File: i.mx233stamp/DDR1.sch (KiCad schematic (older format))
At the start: 15 parts, among them U2 MT46V32M16TG

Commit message: Added some connections to the pin header and the filters of the sources
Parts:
- removed C22, C23, C24, C25, C26, C27, C28, C29: 100nF, 0402, symbol CAP
- removed C30: 1uF, 0603, symbol CAP
- removed RP1, RP2, RP3, RP4, RP5: R_PACK4, R_PACK4-0402, symbol R_PACK4
- added C? (x10): 0.1uF, symbol C
- added C?: 1uF, symbol C
- added R? (x2): 1K 1%, symbol R
- added R?: 47K, symbol R
- added R?: R, symbol R
- added U?: M25P32, symbol M25P32
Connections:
- net labels added: SSPI_CMD, SSPI_DATA0, SSPI_DATA1, SSPI_DATA2, SSPI_DATA3, SSPI_SCK, VDDIO_3V3, VDDM_2V5
- net labels removed: R_DDR_A0, R_DDR_A1, R_DDR_A10, R_DDR_A11, R_DDR_A12, R_DDR_A2, R_DDR_A3, R_DDR_A4, R_DDR_A5, R_DDR_A6, R_DDR_A7, R_DDR_A8, R_DDR_A9
- wire segments 125 -> 136
- no-connect marks 0 -> 7

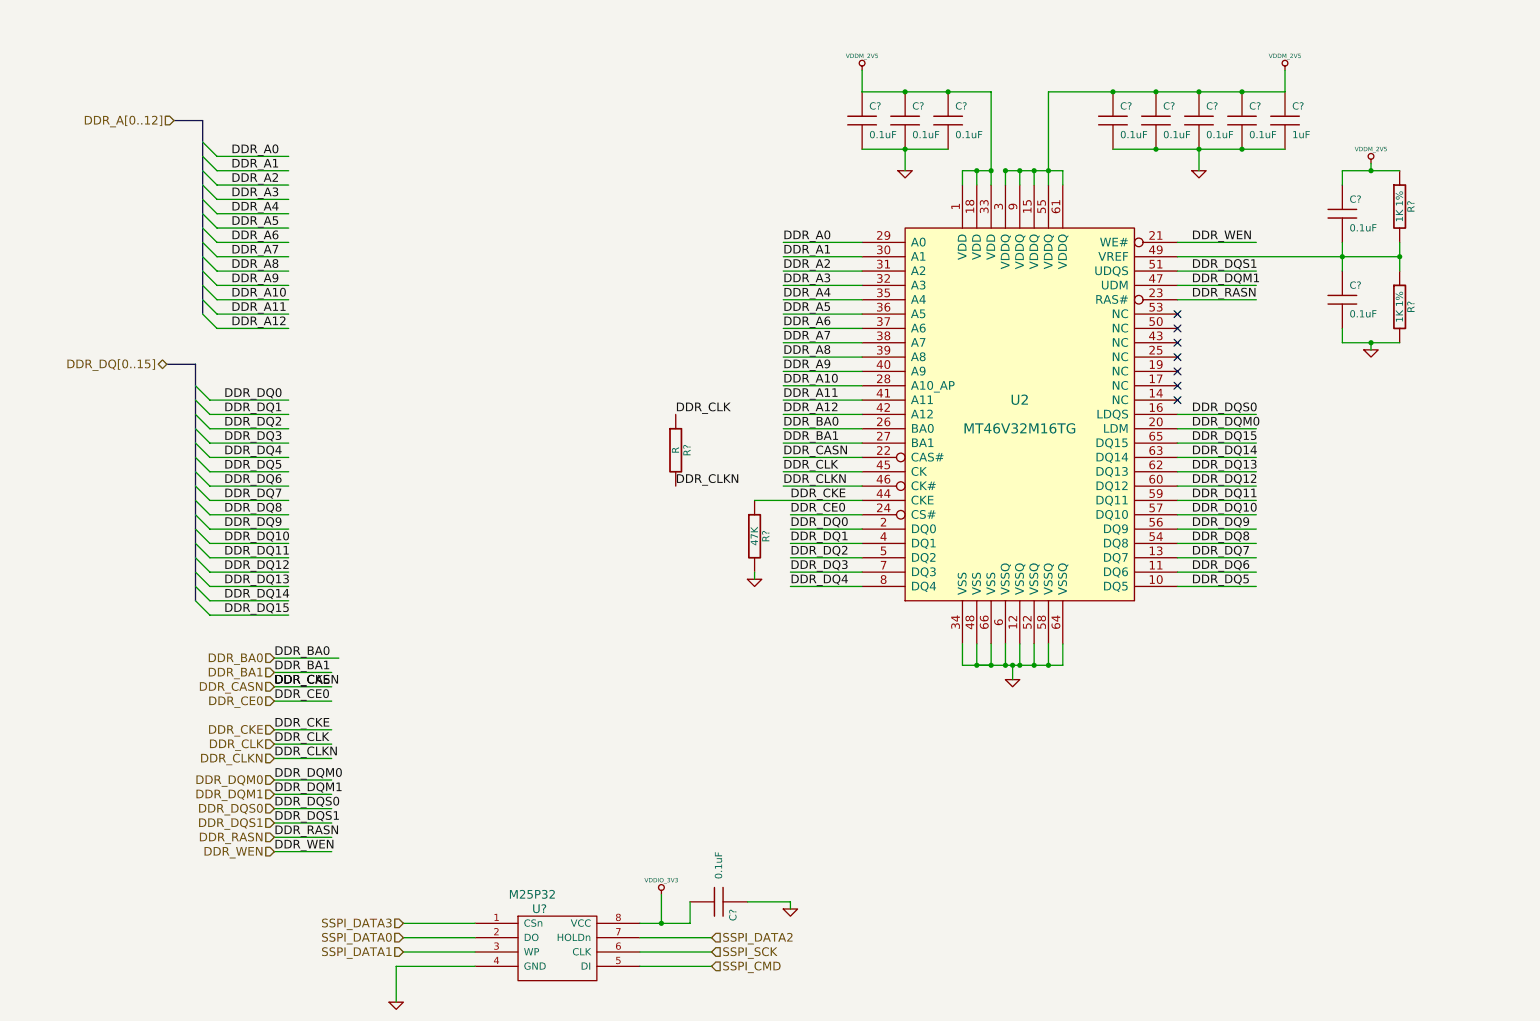
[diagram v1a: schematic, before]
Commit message: Corrected some signals of uSD card
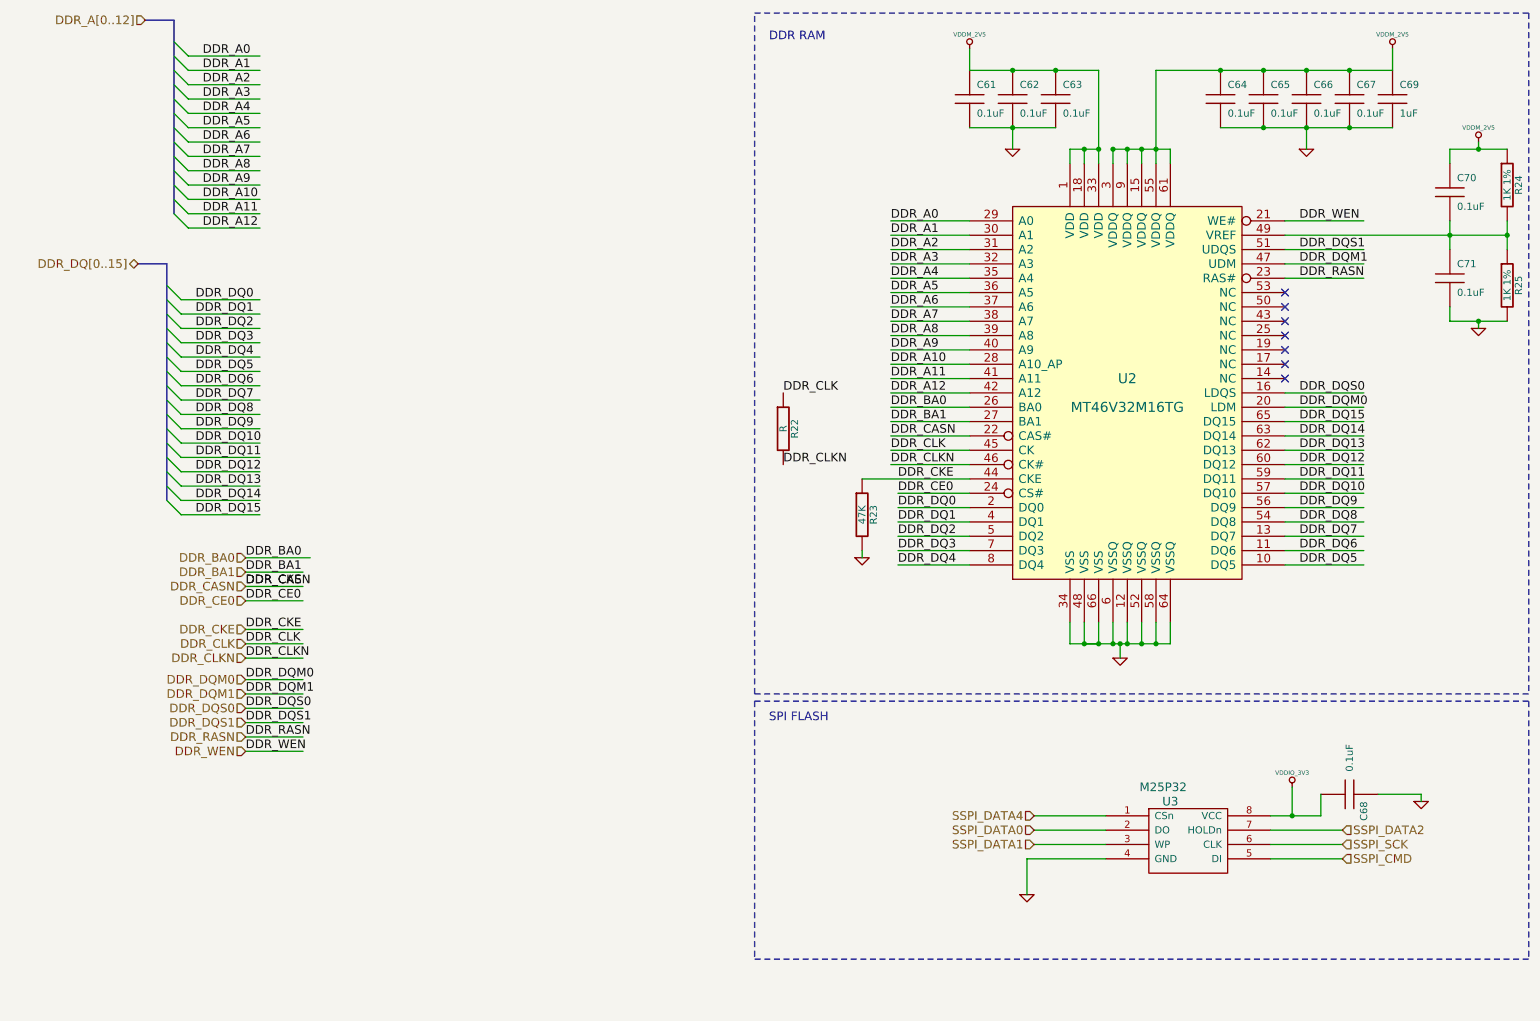
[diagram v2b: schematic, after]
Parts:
- gave numbers to parts that had none: 16
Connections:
- net labels added: SSPI_DATA4
- net labels removed: SSPI_DATA3
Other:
- note added: "DDR RAM"
- note added: "SPI FLASH"
- moved on the sheet: C61, C62, C63, C64, C65, C66, C67, C68, C69, C70, C71, R22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
